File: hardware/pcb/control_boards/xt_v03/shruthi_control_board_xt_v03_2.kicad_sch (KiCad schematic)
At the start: 39 parts, among them IC4 4051, IC5 4051, IC6 4051, IC7 4051

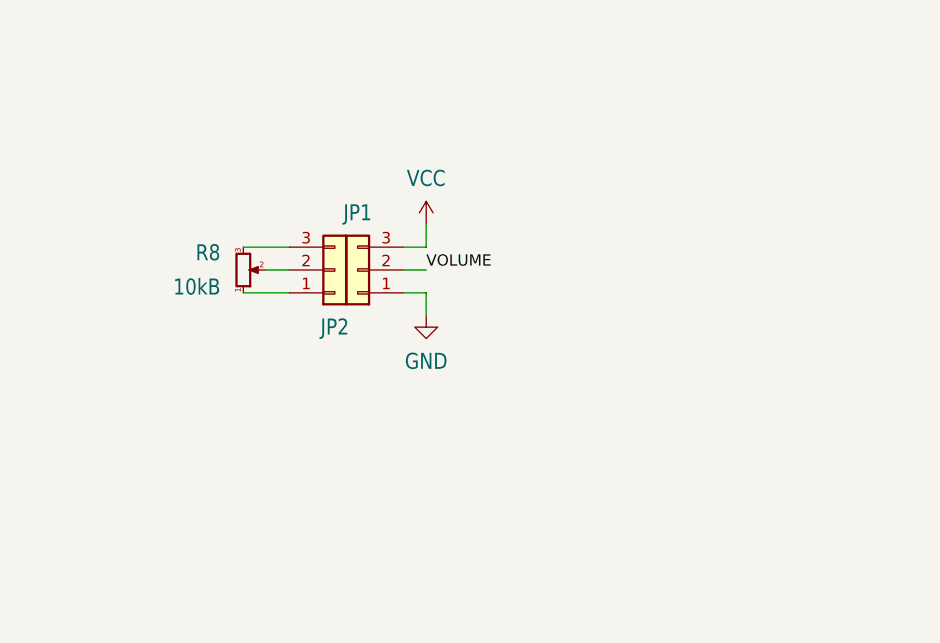
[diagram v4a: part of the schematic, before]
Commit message: update footprint and silkscreen for volume jumpers
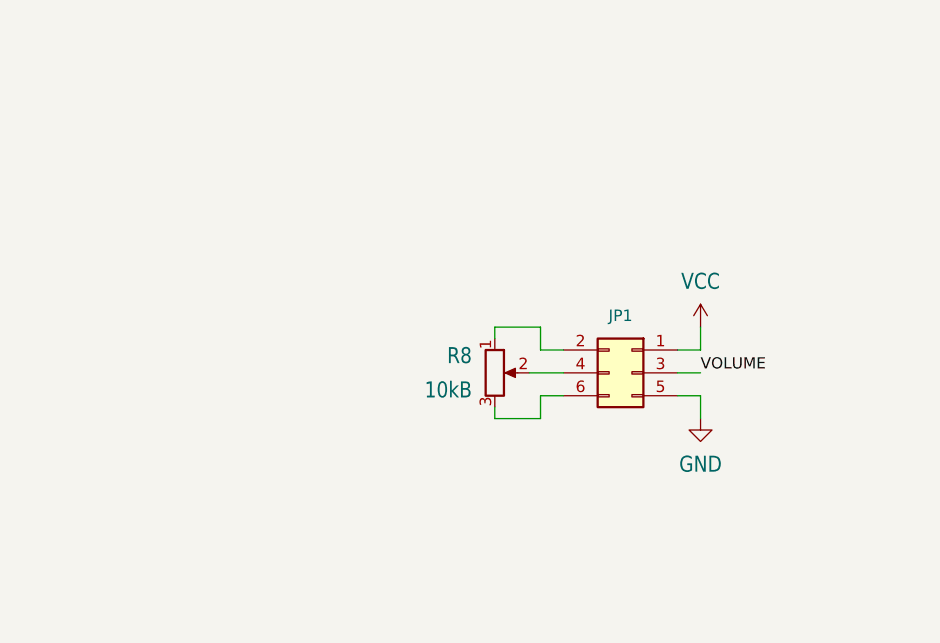
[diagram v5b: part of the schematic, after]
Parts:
- removed JP1, JP2: M03PTH, shruthi_control_board_xt_v03:1X03, symbol Connector_Generic:Conn_01x03
- added JP1: Conn_02x03_Odd_Even, Connector_PinHeader_2.54mm:PinHeader_2x03_P2.54mm_Vertical, symbol Connector_Generic:Conn_02x03_Odd_Even
- R8: symbol Device:R_Potentiometer_Small -> Device:R_Potentiometer
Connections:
- net GND: now also JP1.5 (Pin_5)
- net VCC: now also JP1.1 (Pin_1)
- net VOLUME: now also JP1.3 (Pin_3)
- net at R8.1: now also JP1.2 (Pin_2)
- net at R8.2: now also JP1.4 (Pin_4)
- net at R8.3: now also JP1.6 (Pin_6)
